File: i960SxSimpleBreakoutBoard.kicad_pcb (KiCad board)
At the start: 4 copper layers, 80.1 x 66.6 mm, 26 parts, among them J1 Conn_01x07, J2 Pure Input Pins, J3 Clock, Power, and Bidirection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, J4 Conn_01x05, J5 Multiplexed Address/Data Lines, J6 Upper 16 Address Lines, U1 80960Sx

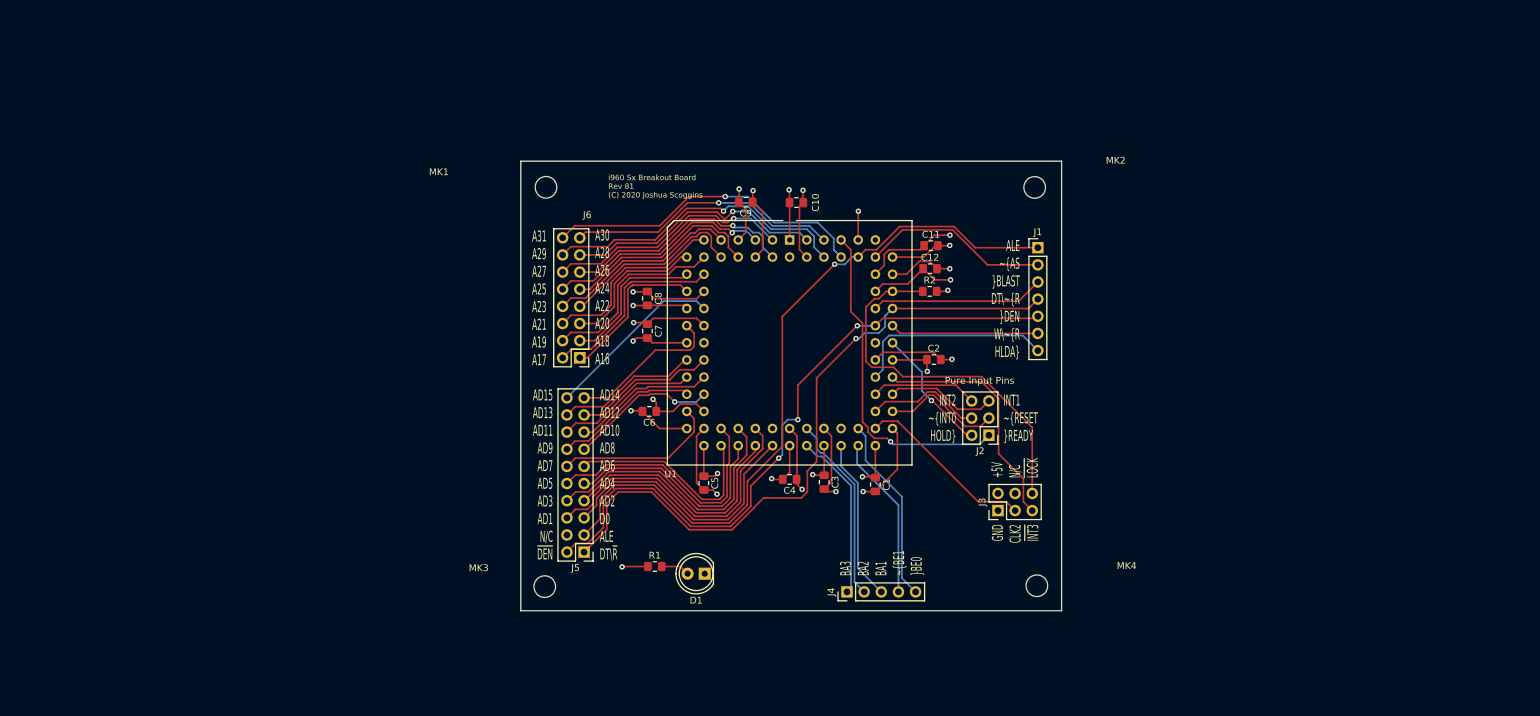
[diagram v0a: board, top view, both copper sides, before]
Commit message: Condense the pin headers further
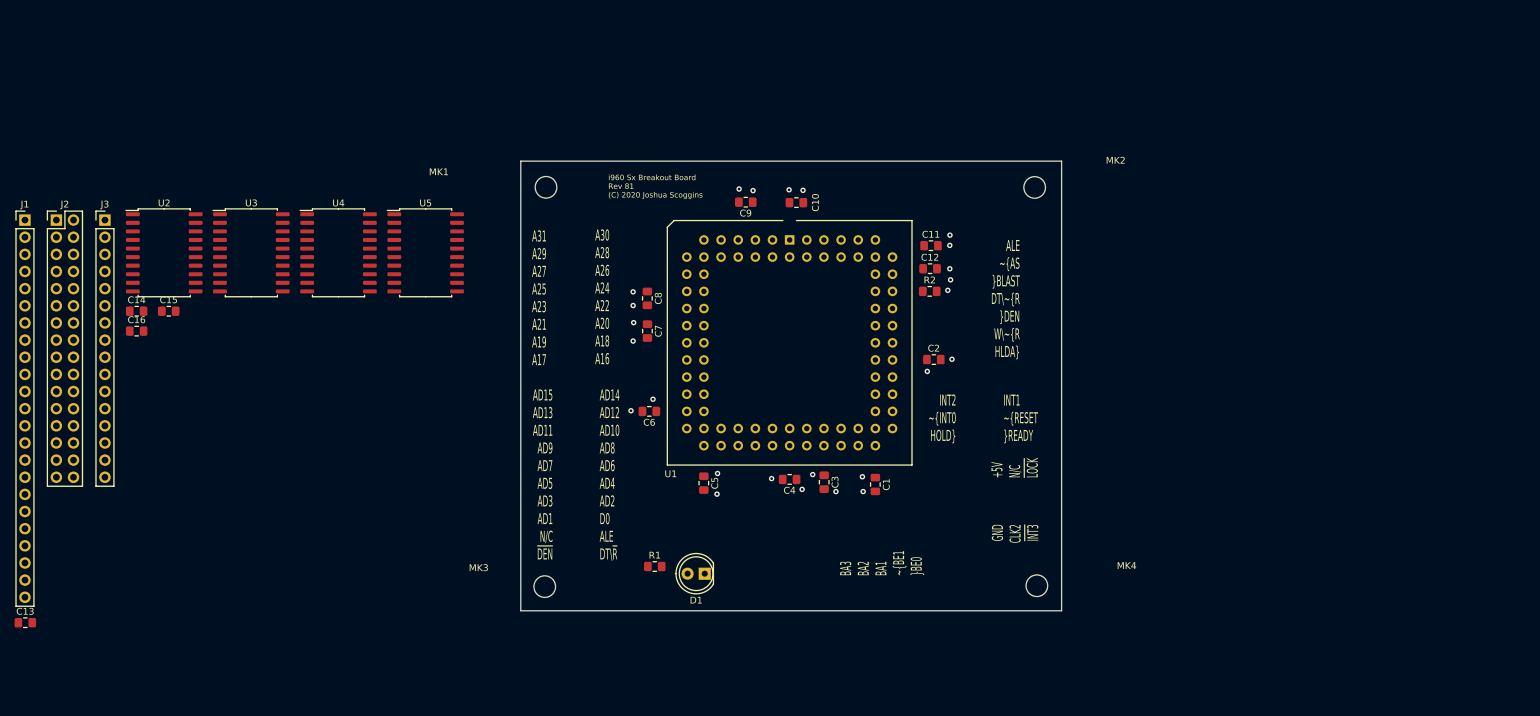
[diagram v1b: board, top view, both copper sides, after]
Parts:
- removed J4: Conn_01x05, Connector_PinHeader_2.54mm:PinHeader_1x05_P2.54mm_Vertical
- removed J5: Multiplexed Address/Data Lines, Connector_PinHeader_2.54mm:PinHeader_2x10_P2.54mm_Vertical
- removed J6: Upper 16 Address Lines, Connector_PinHeader_2.54mm:PinHeader_2x08_P2.54mm_Vertical
- added C13: 0.1uF, Capacitor_SMD:C_0805_2012Metric_Pad1.15x1.40mm_HandSolder, F.Cu at (-112.2, 54.6)
- added C14: 0.1uF, Capacitor_SMD:C_0805_2012Metric_Pad1.15x1.40mm_HandSolder, F.Cu at (-95.7, 8.41)
- added C15: 0.1uF, Capacitor_SMD:C_0805_2012Metric_Pad1.15x1.40mm_HandSolder, F.Cu at (-91.0, 8.41)
- added C16: 0.1uF, Capacitor_SMD:C_0805_2012Metric_Pad1.15x1.40mm_HandSolder, F.Cu at (-95.7, 11.4)
- added U2: 74HC573, Package_SO:SOIC-20W_7.5x12.8mm_P1.27mm, F.Cu at (-91.6, -0.24)
- added U3: 74HC573, Package_SO:SOIC-20W_7.5x12.8mm_P1.27mm, F.Cu at (-78.7, -0.24)
- added U4: 74HC245, Package_SO:SOIC-20W_7.5x12.8mm_P1.27mm, F.Cu at (-65.8, -0.24)
- added U5: 74HC245, Package_SO:SOIC-20W_7.5x12.8mm_P1.27mm, F.Cu at (-52.9, -0.24)
- J1: value Conn_01x07 -> Conn_01x23; footprint Connector_PinHeader_2.54mm:PinHeader_1x07_P2.54mm_Vertical -> Connector_PinHeader_2.54mm:PinHeader_1x23_P2.54mm_Vertical
- J2: value Pure Input Pins -> Conn_02x16_Counter_Clockwise; footprint Connector_PinHeader_2.54mm:PinHeader_2x03_P2.54mm_Vertical -> Connector_PinHeader_2.54mm:PinHeader_2x16_P2.54mm_Vertical
- J3: value Clock, Power, and Bidirectional Pins -> Data Lines; footprint Connector_PinHeader_2.54mm:PinHeader_2x03_P2.54mm_Vertical -> Connector_PinHeader_2.54mm:PinHeader_1x16_P2.54mm_Vertical
- moved J1 150.1 mm to (-112.3, -5.09)
- moved J2 141.8 mm to (-107.6, -5.09), turned to 0 degrees
- moved J3 139.1 mm to (-100.4, -5.09), turned to 0 degrees
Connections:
- J1 pad 3: /~BLAST -> /DT\~R
- J1 pad 4: /DT\~R -> /~DEN
- J1 pad 5: /~DEN -> /W\~R
- J1 pad 6: /W\~R -> /HLDA
- J1 pad 7: /HLDA -> /~BE1
- J2 pad 1: /~READY -> /A0
- J2 pad 2: /HOLD -> /A1
- J2 pad 3: /~RESET -> /A2
- J2 pad 4: /~INT0 -> /A3
- J2 pad 5: /INT1 -> /A4
- J2 pad 6: /INT2 -> /A5
- J3 pad 1: GND -> /D0
- J3 pad 2: +5V -> /D1
- J3 pad 3: /CLK2 -> /D2
- J3 pad 4: Net-(J3-Pad4) -> /D3
- J3 pad 5: /~INT3 -> /D4
- J3 pad 6: /~LOCK -> /D5
- U1 pad 41: /D0 -> /D0'
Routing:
- net GND: track 124.3 -> 0.00 mm, vias 13 -> 12
- net +5V: track 120.5 -> 0.00 mm, vias 14 -> 13
- net /ALE: track 107.1 -> 0.00 mm, vias 1 -> 0
- net /DT\~R: track 99.7 -> 0.00 mm, vias 1 -> 0
- net /~DEN: track 98.5 -> 0.00 mm, vias 3 -> 0
- net /~LOCK: track 55.9 -> 0.00 mm
- net /~READY: track 49.3 -> 0.00 mm, vias 1 -> 0
- net /A31: track 48.5 -> 0.00 mm, vias 1 -> 0
- net /A29: track 46.1 -> 0.00 mm, vias 1 -> 0
- net /AD1: track 44.6 -> 0.00 mm
- net /AD3: track 41.2 -> 0.00 mm
- net /A30: track 40.6 -> 0.00 mm, vias 1 -> 0
- net /D0: track 40.2 -> 0.00 mm
- net /A28: track 38.9 -> 0.00 mm, vias 1 -> 0
- net /AD5: track 38.3 -> 0.00 mm
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- removed copper zone on In1.Cu, net +5V
- removed copper zone on In2.Cu, net GND

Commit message: Widen the board to make routing easier
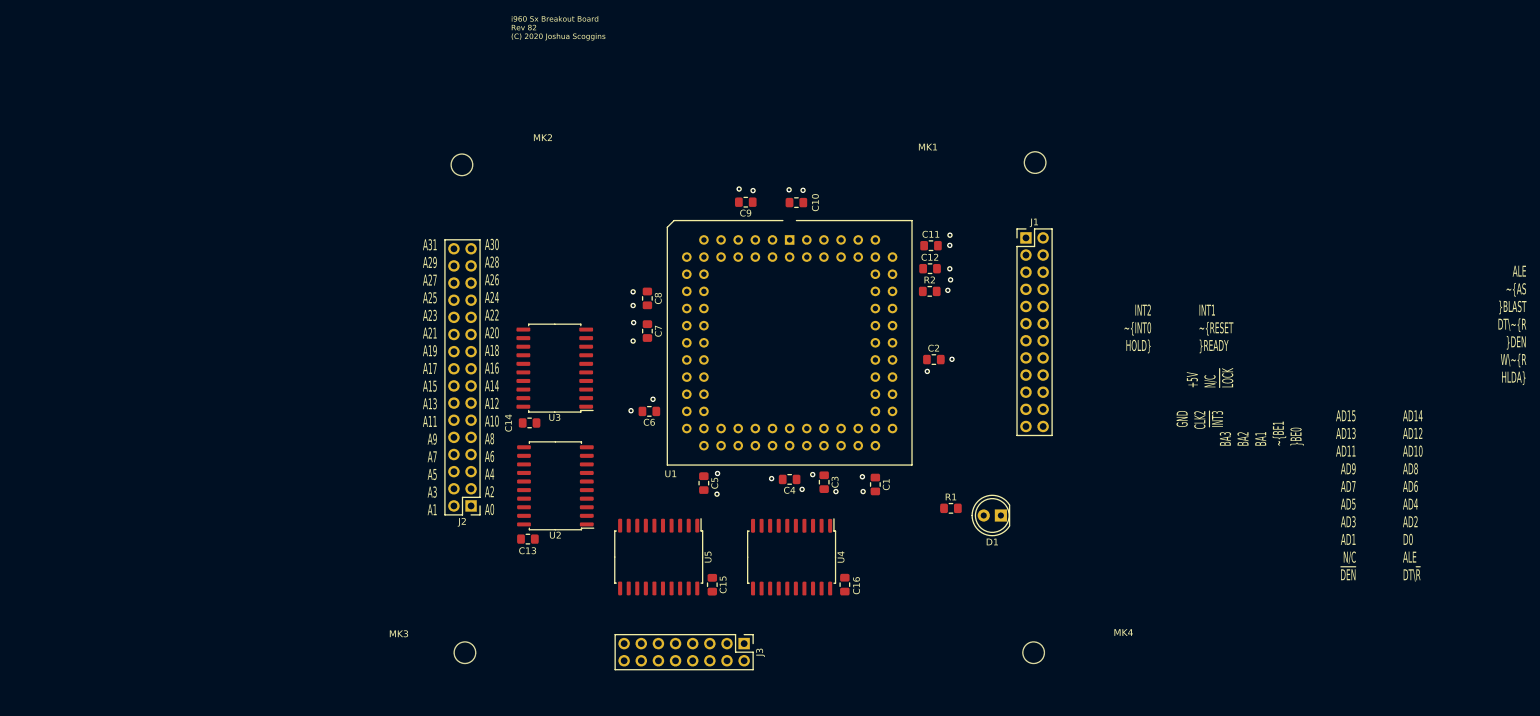
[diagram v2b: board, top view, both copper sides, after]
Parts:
- J1: value Conn_01x23 -> Control Lines; footprint Connector_PinHeader_2.54mm:PinHeader_1x23_P2.54mm_Vertical -> Connector_PinHeader_2.54mm:PinHeader_2x12_P2.54mm_Vertical
- J2: value Conn_02x16_Counter_Clockwise -> Address Lines
- J3: footprint Connector_PinHeader_2.54mm:PinHeader_1x16_P2.54mm_Vertical -> Connector_PinHeader_2.54mm:PinHeader_2x08_P2.54mm_Vertical
- moved J1 148.3 mm to (36.1, -2.45)
- moved J3 113.6 mm to (-5.70, 57.7), turned to 270 degrees
- moved C16 111.4 mm to (9.22, 48.9), turned to 90 degrees
- moved C15 90.1 mm to (-10.4, 48.9), turned to 90 degrees
- moved MK2 84.9 mm to (-47.5, -13.3)
- moved U4 80.9 mm to (1.33, 44.8), turned to 270 degrees
- moved C13 75.5 mm to (-37.7, 42.2)
- moved J2 74.6 mm to (-46.2, 37.3), turned to 180 degrees
- moved MK1 72.6 mm to (37.4, -13.6)
- moved U2 67.5 mm to (-33.7, 34.3), turned to 180 degrees
- moved C14 60.5 mm to (-37.5, 25.0)
- moved U5 56.8 mm to (-18.4, 44.8), turned to 270 degrees
- moved U3 48.1 mm to (-33.8, 16.8), turned to 180 degrees
- moved D1 44.7 mm to (32.3, 38.7)
- moved R1 44.7 mm to (24.9, 37.6)
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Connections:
- J1 pad 23: +5V -> GND
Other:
- board outline removed
- board text added: "A30 A28 A26 A24 A22 A20 A18 A16 A14 A12 A10 A8 A6 A4 A2 A0"
- board text added: "A31 A29 A27 A25 A23 A21 A19 A17 A15 A13 A11 A9 A7 A5 A3 A1"
- board text added: "i960 Sx Breakout Board Rev 82 (C) 2020 Joshua Scoggins"
- board text removed: "A30 A28 A26 A24 A22 A20 A18 A16"
- board text removed: "A31 A29 A27 A25 A23 A21 A19 A17"
- board text removed: "i960 Sx Breakout Board Rev 81 (C) 2020 Joshua Scoggins"

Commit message: Use single row headers in all cases now
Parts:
- J1: value Control Lines -> Conn_01x23; footprint Connector_PinHeader_2.54mm:PinHeader_2x12_P2.54mm_Vertical -> Connector_PinHeader_2.54mm:PinHeader_1x23_P2.54mm_Vertical
- J2: footprint Connector_PinHeader_2.54mm:PinHeader_2x16_P2.54mm_Vertical -> Connector_PinHeader_2.54mm:PinHeader_1x32_P2.54mm_Vertical
- J3: footprint Connector_PinHeader_2.54mm:PinHeader_2x08_P2.54mm_Vertical -> Connector_PinHeader_2.54mm:PinHeader_1x16_P2.54mm_Vertical
- moved J3 16.1 mm to (10.3, 59.8)
- moved J2 14.5 mm to (-46.8, 51.7)
- moved J1 5.12 mm to (37.6, -7.33)
- renumbered U2 to U1, U3 to U2, U1 to U3
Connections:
- J1 pad 23: GND -> +5V

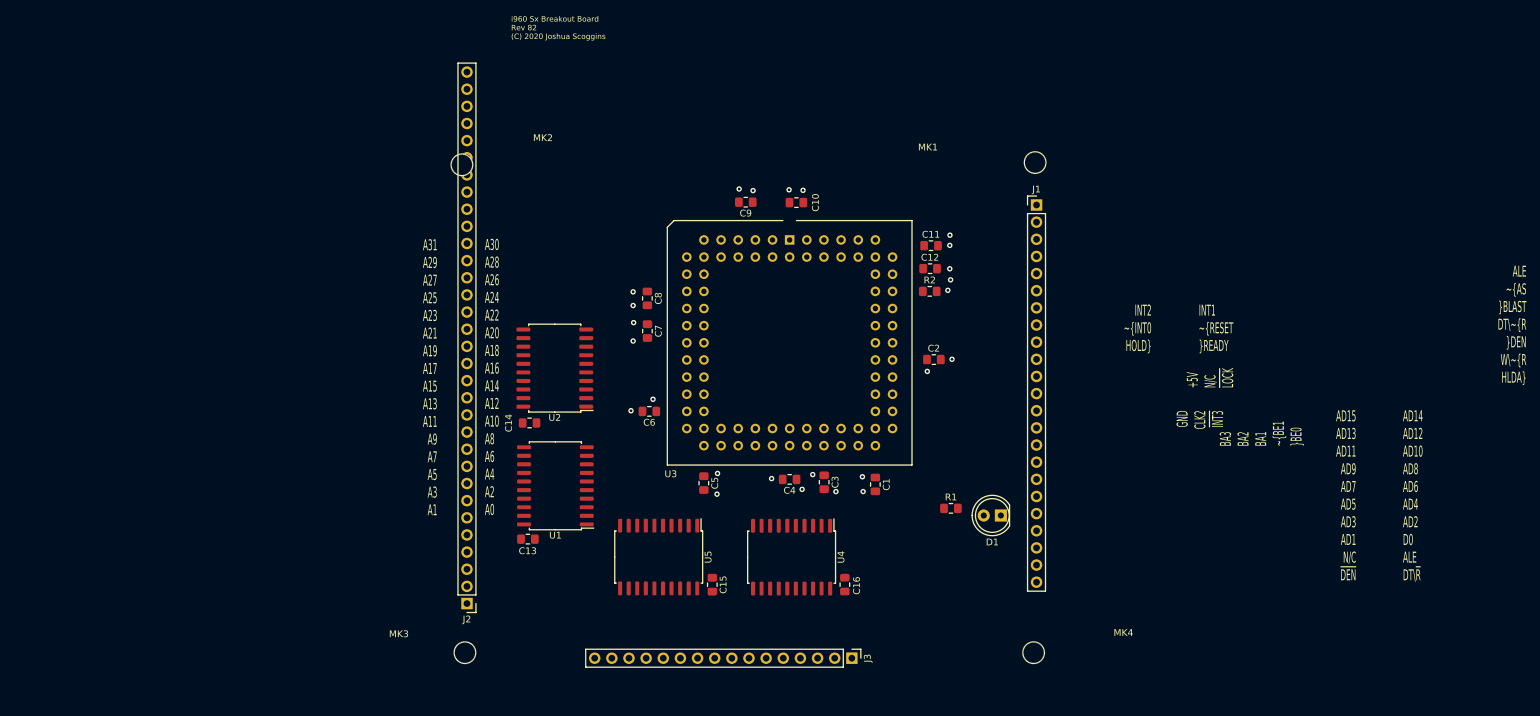
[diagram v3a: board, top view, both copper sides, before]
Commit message: Modify pinout of control signals to make routing of traces easier
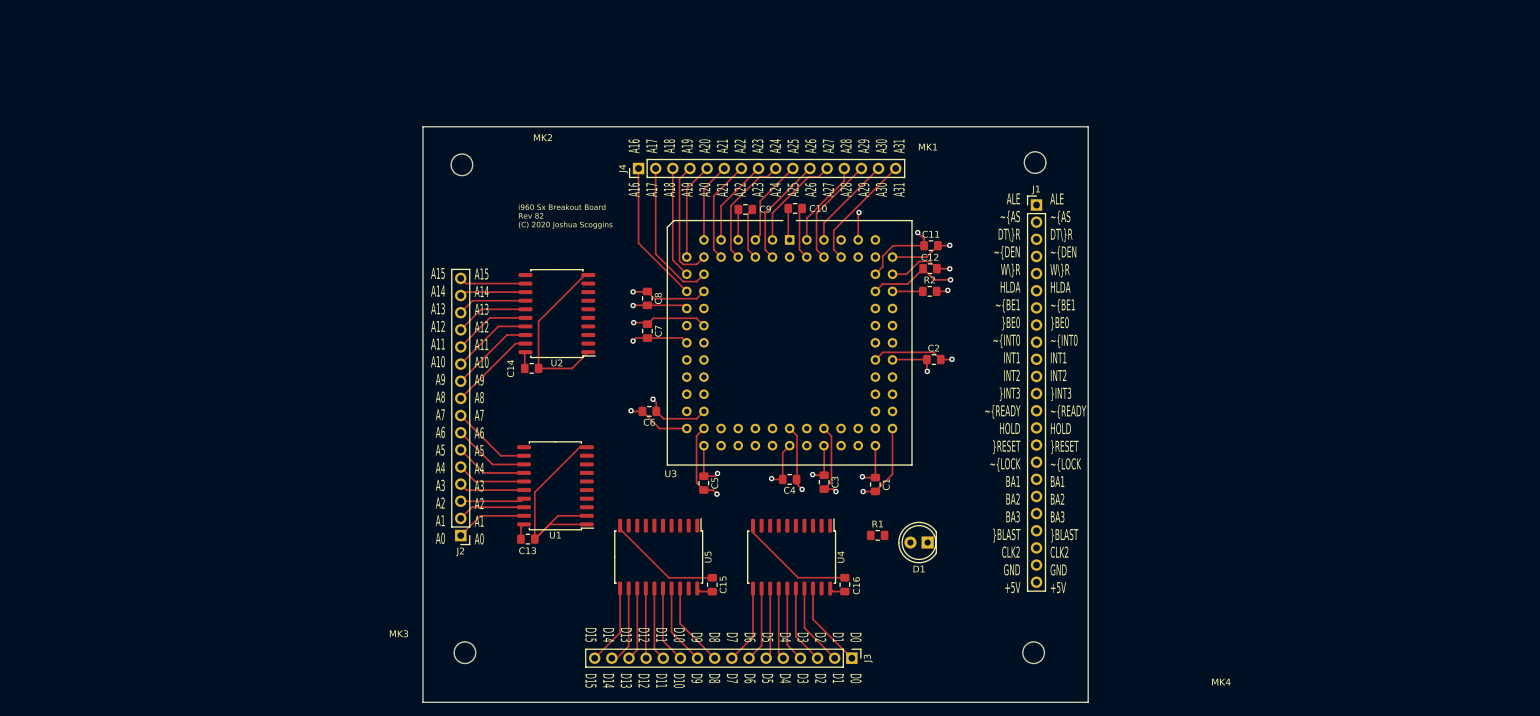
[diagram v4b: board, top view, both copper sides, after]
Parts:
- added J4: Address Lines Upper, Connector_PinHeader_2.54mm:PinHeader_1x16_P2.54mm_Vertical, F.Cu at (-21.3, -12.7)
- J2: value Address Lines -> Address Lines Lower; footprint Connector_PinHeader_2.54mm:PinHeader_1x32_P2.54mm_Vertical -> Connector_PinHeader_2.54mm:PinHeader_1x16_P2.54mm_Vertical
- moved D1 11.6 mm to (21.5, 42.7)
- moved R1 11.6 mm to (14.1, 41.6)
- moved J2 10.1 mm to (-47.7, 41.6)
- moved C14 8.09 mm to (-37.2, 16.9)
- moved U2 8.09 mm to (-33.4, 8.76)
- moved C9 1.07 mm to (-5.52, -6.67)
- moved C10 0.89 mm to (1.85, -6.82)
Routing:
- net GND: track 0.00 -> 212.1 mm, vias 12 -> 11
- net +5V: track 0.00 -> 118.3 mm, vias 13 -> 11
- net /A17: track 0.00 -> 22.0 mm
- net /A16: track 0.00 -> 21.2 mm
- net /A19: track 0.00 -> 18.6 mm
- net /A31: track 0.00 -> 17.4 mm
- net /A24: track 0.00 -> 17.0 mm
- net /A18: track 0.00 -> 16.5 mm
- net /A29: track 0.00 -> 16.3 mm
- net /A26: track 0.00 -> 16.3 mm
- net /A22: track 0.00 -> 15.3 mm
- net /A27: track 0.00 -> 14.8 mm
- net /A20: track 0.00 -> 14.4 mm
- net /A30: track 0.00 -> 13.9 mm
- net /A8: track 0.00 -> 13.0 mm
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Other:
- board outline added: 98.6 x 85.3 mm
- board text added: "A15 A14 A13 A12 A11 A10 A9 A8 A7 A6 A5 A4 A3 A2 A1 A0"
- board text added: "A16 A17 A18 A19 A20 A21 A22 A23 A24 A25 A26 A27 A28 A29 A30 A31"
- board text added: "ALE ~AS DT\~R ~DEN W\~R HLDA ~BE1 ~BE0 ~INT0 INT1 INT2 ~INT3 ~READY HOLD ~RESET ~LOCK BA1 BA2 BA3 ~BLAST CLK2 GND +5V"
- board text added: "D0 D1 D2 D3 D4 D5 D6 D7 D8 D9 D10 D11 D12 D13 D14 D15"
- board text removed: "+5V N/C ~LOCK"
- board text removed: "A30 A28 A26 A24 A22 A20 A18 A16 A14 A12 A10 A8 A6 A4 A2 A0"
- board text removed: "A31 A29 A27 A25 A23 A21 A19 A17 A15 A13 A11 A9 A7 A5 A3 A1"
- board text removed: "AD14 AD12 AD10 AD8 AD6 AD4 AD2 D0 ALE DT\~R"
- board text removed: "AD15 AD13 AD11 AD9 AD7 AD5 AD3 AD1 N/C ~DEN"
- board text removed: "ALE ~AS ~BLAST DT\~R ~DEN W\~R HLDA"
- board text removed: "BA3 BA2 BA1 ~BE1 ~BE0"
- board text removed: "GND CLK2 ~INT3"
- board text removed: "INT1 ~RESET ~READY"
- board text removed: "INT2 ~INT0 HOLD"
